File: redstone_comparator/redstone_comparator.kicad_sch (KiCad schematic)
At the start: 72 parts, among them J1 1x4_Pogo, J2 1x4_Pogo, J3 1x4_Pogo, J4 1x4_Pogo, J5 1x4_Pogo, J6 1x4_Pogo, J7 1x4_Pogo, J8 1x4_Pogo, J9 2.54mm_ProgrammingPin, Q1 MMBT3904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

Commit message: finalize initial comparator design
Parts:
- removed D10, D11, D12, D13, D14, D15, D16, D4, D5, D6, D7, D8, D9: LED, SamacSys_Parts:LEDC1608X115N, symbol Device:LED
- removed Q4: MMBT3904, Package_TO_SOT_SMD:SOT-23, symbol Transistor_BJT:MMBT3904
- removed R10, R11, R12, R13, R14, R15, R16, R4, R5, R6, R7, R8, R9: 200, SamacSys_Parts:CRCW1210200RJNEAIF, symbol Device:R_Small
- removed R21: 1k, SamacSys_Parts:ERJ-UP6D1001V, symbol Device:R_Small
- D1, D2, D3: footprint SamacSys_Parts:LEDC1608X115N -> LED_THT:LED_D3.0mm
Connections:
- net at D1.1 (K), Q1.3 (C): no longer D2.1 (K), D3.1 (K)
- net at Q2.3 (C): now also D2.1 (K)
- net at Q3.3 (C): now also D3.1 (K)
- no-connect marks 31 -> 32
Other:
- moved on the sheet: D1, D2, D3, Q1, Q3, R1, R2, R3

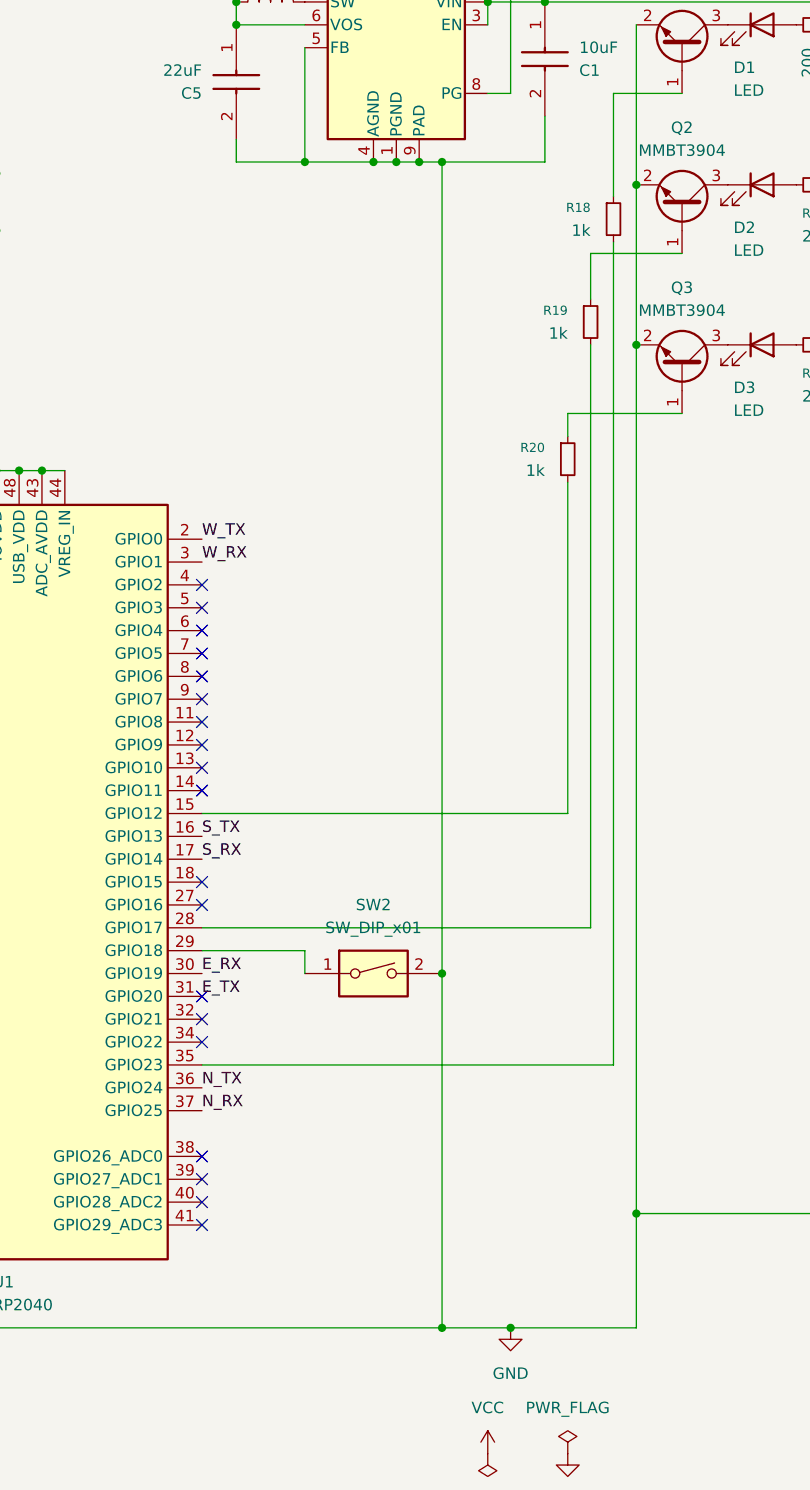
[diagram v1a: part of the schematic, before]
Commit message: finish routing all connections, todo align components and make it symmetric
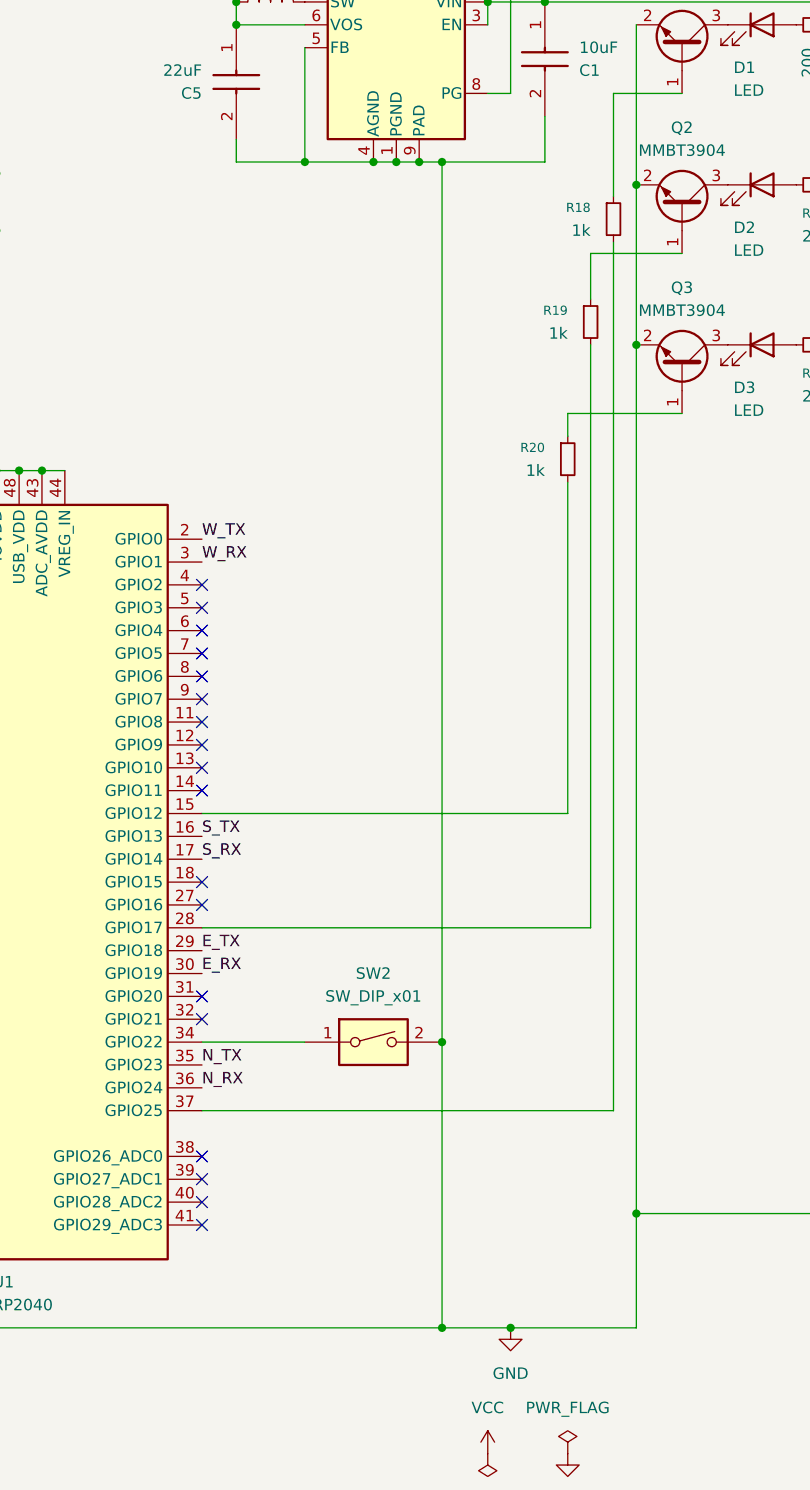
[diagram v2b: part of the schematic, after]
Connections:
- net E_TX: now also U1.29 (GPIO18); no longer U1.31 (GPIO20)
- net N_RX: now also U1.36 (GPIO24); no longer U1.37 (GPIO25)
- net N_TX: now also U1.35 (GPIO23); no longer U1.36 (GPIO24)
- net at R18.2: now also U1.37 (GPIO25); no longer U1.35 (GPIO23)
- net at SW2.1: now also U1.34 (GPIO22); no longer U1.29 (GPIO18)
- no-connect marks 32 -> 31
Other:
- moved on the sheet: SW2
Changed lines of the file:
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@@
 	)
 	(junction
-		(at 154.94 134.62)
+		(at 154.94 142.24)
 		(diameter 0)
 		(color 0 0 0 1)
@@
 	)
 	(no_connect
-		(at 128.27 137.16)
-	)
-	(no_connect
 		(at 77.47 93.98)
 	)
 	(no_connect
-		(at 128.27 142.24)
+		(at 128.27 137.16)
 	)
 	(no_connect
@@
 	(wire
 		(pts
-			(xy 139.7 132.08) (xy 139.7 134.62)
-		)
-		(stroke
-			(width 0)
-			(type default)
-		)
-	)
-	(wire
-		(pts
 			(xy 260.35 85.09) (xy 260.35 95.25)
 		)
@@
 	(wire
 		(pts
-			(xy 154.94 44.45) (xy 154.94 134.62)
-		)
-		(stroke
-			(width 0)
-			(type default)
-			(color 0 0 0 1)
-		)
-	)
-	(wire
-		(pts
 			(xy 82.55 59.69) (xy 82.55 67.31)
 		)
@@
 	(wire
 		(pts
-			(xy 128.27 132.08) (xy 139.7 132.08)
+			(xy 128.27 142.24) (xy 139.7 142.24)
 		)
 		(stroke
@@
 	(wire
 		(pts
-			(xy 173.99 144.78) (xy 128.27 144.78)
+			(xy 173.99 149.86) (xy 128.27 149.86)
 		)
 		(stroke
@@
 	(wire
 		(pts
-			(xy 154.94 134.62) (xy 154.94 173.99)
-		)
-		(stroke
-			(width 0)
-			(type default)
-			(color 0 0 0 1)
-		)
-	)
-	(wire
-		(pts
 			(xy 199.39 57.15) (xy 199.39 64.77)
 		)
@@
 	(wire
 		(pts
+			(xy 154.94 44.45) (xy 154.94 142.24)
+		)
+		(stroke
+			(width 0)
+			(type default)
+			(color 0 0 0 1)
+		)
+	)
+	(wire
+		(pts
 			(xy 168.91 72.39) (xy 181.61 72.39)
 		)
@@
 	(wire
 		(pts
+			(xy 154.94 142.24) (xy 154.94 173.99)
+		)
+		(stroke
+			(width 0)
+			(type default)
+			(color 0 0 0 1)
+		)
+	)
+	(wire
+		(pts
 			(xy 22.86 173.99) (xy 62.23 173.99)
 		)
@@
 	(wire
 		(pts
-			(xy 173.99 53.34) (xy 173.99 144.78)
+			(xy 173.99 53.34) (xy 173.99 149.86)
 		)
 		(stroke
@@
 	)
 	(label "N_RX"
-		(at 128.27 149.86 0)
+		(at 128.27 147.32 0)
 		(effects
 			(font
@@
 	)
 	(label "N_TX"
-		(at 128.27 147.32 0)
+		(at 128.27 144.78 0)
 		(effects
 			(font
@@
 	)
 	(label "E_TX"
-		(at 128.27 137.16 0)
+		(at 128.27 132.08 0)
 		(effects
 			(font
@@
 	(symbol
 		(lib_id "Switch:SW_DIP_x01")
-		(at 147.32 134.62 0)
+		(at 147.32 142.24 0)
 		(unit 1)
 		(exclude_from_sim no)
@@
 		(fields_autoplaced yes)
 		(property "Reference" "SW2"
-			(at 147.32 127 0)
+			(at 147.32 134.62 0)
 			(effects
 				(font
@@
 		)
 		(property "Value" "SW_DIP_x01"
-			(at 147.32 129.54 0)
+			(at 147.32 137.16 0)
 			(effects
 				(font
@@
 		)
 		(property "Footprint" "SamacSys_Parts:416131160801"
-			(at 147.32 134.62 0)
+			(at 147.32 142.24 0)
 			(effects
 				(font
@@
 		)
 		(property "Datasheet" "~"
-			(at 147.32 134.62 0)
+			(at 147.32 142.24 0)
 			(effects
 				(font
@@
 		)
 		(property "Description" "1x DIP Switch, Single Pole Single Throw (SPST) switch, small symbol"
-			(at 147.32 134.62 0)
+			(at 147.32 142.24 0)
 			(effects
 				(font
